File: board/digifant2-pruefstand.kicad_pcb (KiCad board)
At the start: 2 copper layers, 144 x 169 mm, 63 parts, among them J0 VW ECU HARNESS, J1 12V BENCH IN, J2 IDLE VALVE N71, J3 OLED / UI I2C, Q1 2N7002, Q2 P-MOS -30V >=5A, Q3 2N7002, Q5 2N7002, SW1 PUSH, SW2 PUSH, SW3 PUSH, U1 INA226 (0x40), U2 MCP4728 (0x60), U3 INA226 (0x41), U4 AD9833, U5 Raspberry Pi Pico, U6 TS5A3159A, U7 TS5A3159A, U8 TS5A3159A, Y1 25MHz

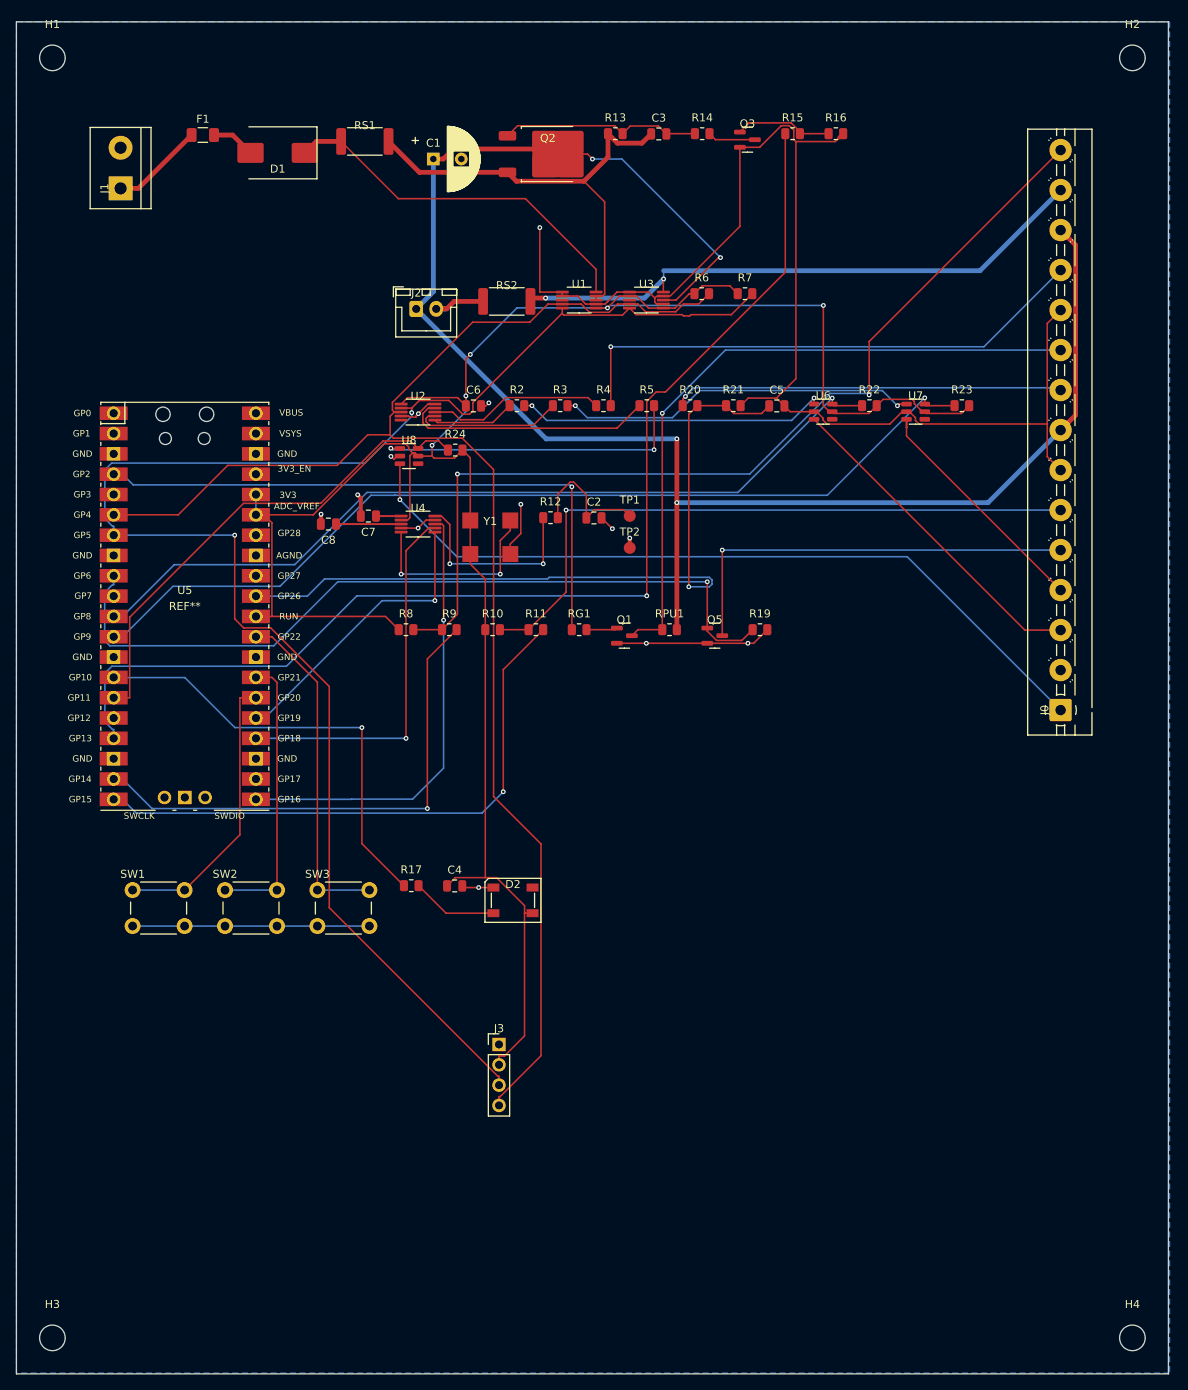
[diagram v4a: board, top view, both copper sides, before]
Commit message: Add 12 scope-probe test points (TP3-TP14) for firmware debugging
Bare 1.5mm test pads (same TestPoint_Pad_D1.5mm footprint as the knock
output's TP1/TP2) on the signals most likely to get probed while
debugging: crank drive, idle-switch drive, ignition/injector capture,
the AD9833 SPI bus (CS/SCK/MOSI), the I2C bus (SDA/SCL), the status LED
data line, and both 12V rails (sensed + switched).

Placement used an automated collision check (footprint + track distance)
against the real board, not manual trial and error -- 12 of 13 originally
attempted points cleared on the first or second pass. +3V3 was dropped
after 4 different anchor attempts (3 different Pico pins, then a
decoupling cap elsewhere) all routed through the same congested corridor
near the Pico; not worth forcing given +3V3 is already exposed at many
existing component pins.

Added digifant2_pruefstand.py's debug_test_points() and spliced the
corresponding schematic symbols/labels into the committed schematic
(verified ERC-clean and schematic-PCB parity unchanged from baseline) --
same lesson as the RS2 fix: a PCB-only addition would silently disappear
on the next schematic sync.

One real residual: TP12 (LED data) reopened a shorting_items/clearance
pair against GND. The actual pad-to-pad distances involved are ~2mm --
nowhere near a real clearance violation -- so the true conflict is
somewhere along the newly-routed copper itself, not locatable precisely
by script. Left for the same manual-nudge treatment as this board's
other tight pockets; KiCad's interactive router will show the exact
offending trace visually.

Co-Authored-By: Claude Sonnet 5 <noreply@anthropic.com>
Claude-Session: https://claude.ai/code/session_01XcEuUwwCT37oProAm8HYeY
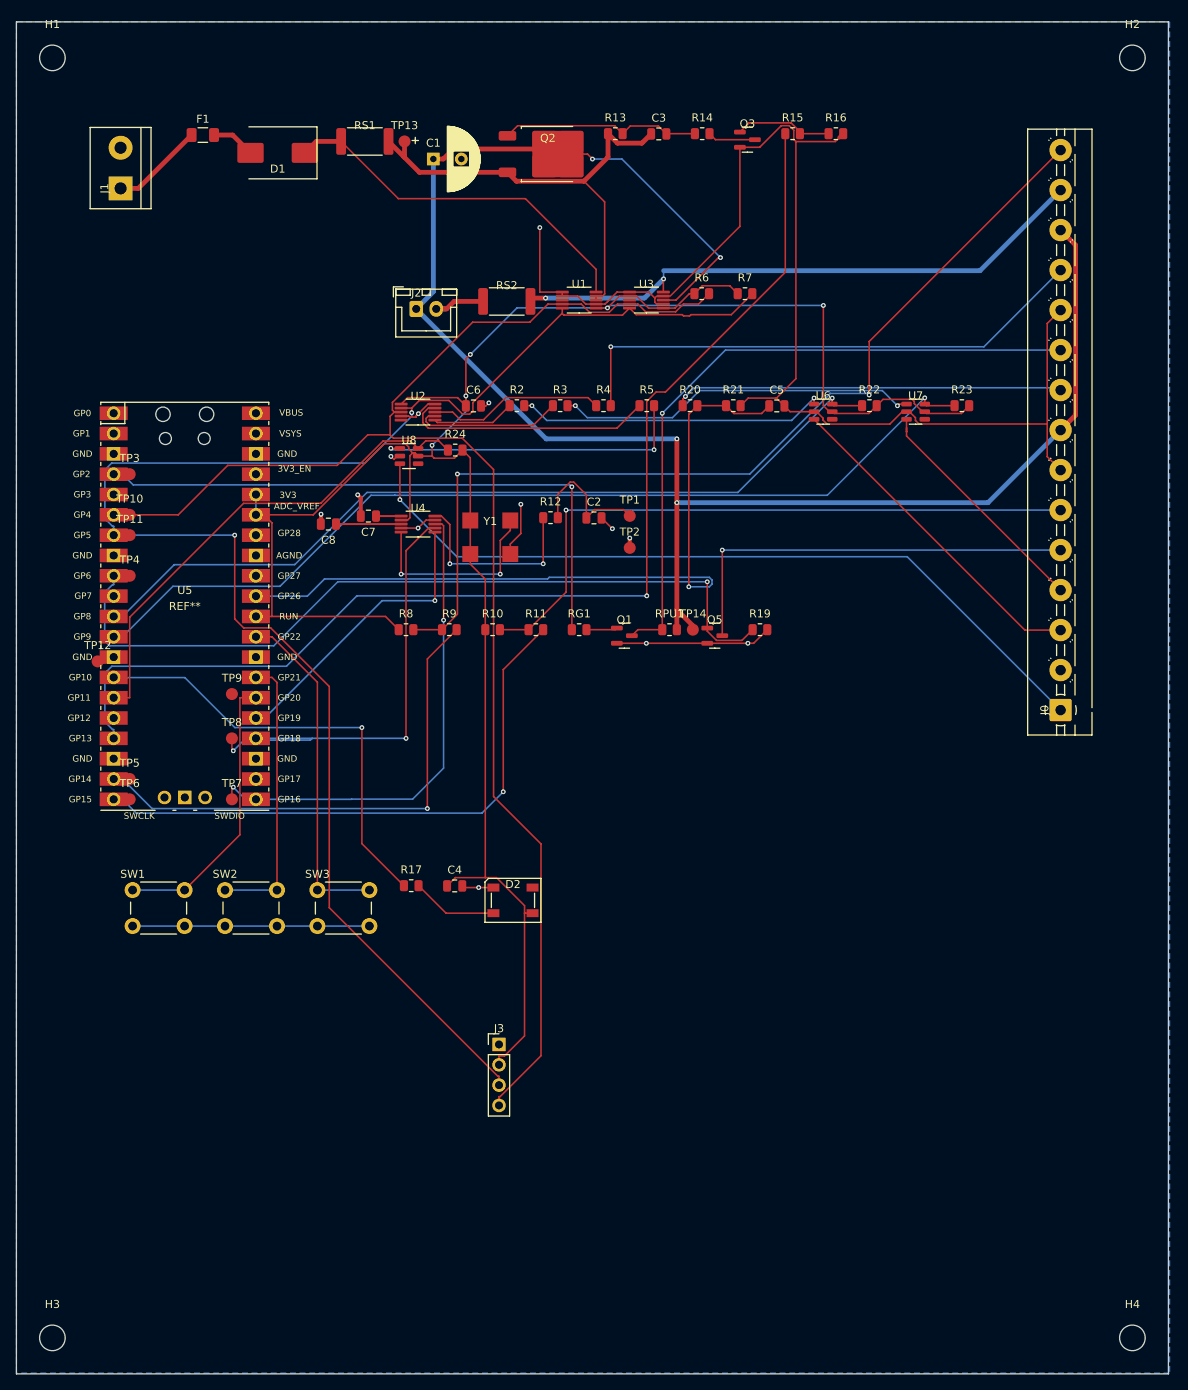
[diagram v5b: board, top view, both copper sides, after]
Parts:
- added TP10: TP I2C_SDA, TestPoint:TestPoint_Pad_D1.5mm, F.Cu at (14.2, 61.6)
- added TP11: TP I2C_SCL, TestPoint:TestPoint_Pad_D1.5mm, F.Cu at (14.2, 64.2)
- added TP12: TP GP10_LED_DATA, TestPoint:TestPoint_Pad_D1.5mm, F.Cu at (10.2, 79.9)
- added TP13: TP +12V_ECU, TestPoint:TestPoint_Pad_D1.5mm, F.Cu at (48.5, 14.9)
- added TP14: TP +12V_ECU_SW, TestPoint:TestPoint_Pad_D1.5mm, F.Cu at (84.6, 76.0)
- added TP3: TP GP2_CRANK, TestPoint:TestPoint_Pad_D1.5mm, F.Cu at (14.2, 56.5)
- added TP4: TP GP6_THROTTLE_IDLE_SW, TestPoint:TestPoint_Pad_D1.5mm, F.Cu at (14.2, 69.2)
- added TP5: TP GP14_IGN_CAPTURE, TestPoint:TestPoint_Pad_D1.5mm, F.Cu at (14.2, 94.6)
- added TP6: TP GP15_INJ_CAPTURE, TestPoint:TestPoint_Pad_D1.5mm, F.Cu at (14.2, 97.2)
- added TP7: TP GP16_SPI_CS, TestPoint:TestPoint_Pad_D1.5mm, F.Cu at (26.9, 97.2)
- added TP8: TP GP18_SPI_SCK, TestPoint:TestPoint_Pad_D1.5mm, F.Cu at (26.9, 89.6)
- added TP9: TP GP19_SPI_MOSI, TestPoint:TestPoint_Pad_D1.5mm, F.Cu at (26.9, 84.0)
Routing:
- net GP18_SPI_SCK: track 47.0 -> 59.1 mm, vias 1 -> 2
- net GP16_SPI_CS: track 56.5 -> 61.6 mm, vias 1 -> 2
- net +12V_ECU_SW: track 220.6 -> 223.9 mm
- net GP6_THROTTLE_IDLE_SW: track 100.4 -> 102.4 mm
- net GP2_CRANK: track 75.8 -> 77.8 mm
- net GP15_INJ_CAPTURE: track 72.8 -> 74.8 mm
- net GP14_IGN_CAPTURE: track 64.6 -> 66.6 mm
- net I2C_SCL: track 204.0 -> 206.0 mm
- net +12V_ECU: track 56.9 -> 58.8 mm
- net VW_PIN10: track 30.4 -> 29.8 mm

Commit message: Fix test points: real THT footprint, and move 10 out from under the Pico
Two real defects caught by user review of the previous commit:

1. All 14 test points (TP1-TP14) used TestPoint_Pad_D1.5mm, a bare SMD
   pad with no drill -- not THT as documented/intended. Switched to
   TestPoint_THTPad_D1.5mm_Drill0.7mm (real 0.7mm hole), vendored the
   footprint, and updated fetch_libs.sh.

2. TP3-TP12 were anchored right at their signal's own Pico pin, which
   placed 10 of the 12 physically *underneath* the Pico module's real
   footprint courtyard (x:[10,32.1] y:[47,99.1]) -- completely
   unreachable with a probe once the module is soldered on. Moved them
   to the clear margin strip west of the Pico (x=5mm), verified against
   real board-edge and courtyard geometry, not just pad/track proximity.

Along the way, found and fixed a real bug in this session's own PCB
scripts: pcbnew.FOOTPRINT(template) clones inherit the template's UUID
unless explicitly reset, so every footprint cloned this way (C7/C8, and
all of TP1-TP14, since they were all cloned from one template) shared a
UUID with its siblings. This doesn't break electrical connectivity but
corrupts DRC's item-identity tracking -- several "violations" this
session were real defects reported against the wrong footprint (one
report cited two parts 70mm apart as a courtyard overlap). Fixed with
ResetUuid() on every affected footprint and pad. With correct UUIDs,
DRC now correctly identified two genuine issues (TP1 too close to a
VW_PIN12 trace once it had a real drill hole; TP13's courtyard actually
overlapping RS1's) that had been reported against the wrong parts
before -- both repositioned and reverified.

Co-Authored-By: Claude Sonnet 5 <noreply@anthropic.com>
Claude-Session: https://claude.ai/code/session_01XcEuUwwCT37oProAm8HYeY
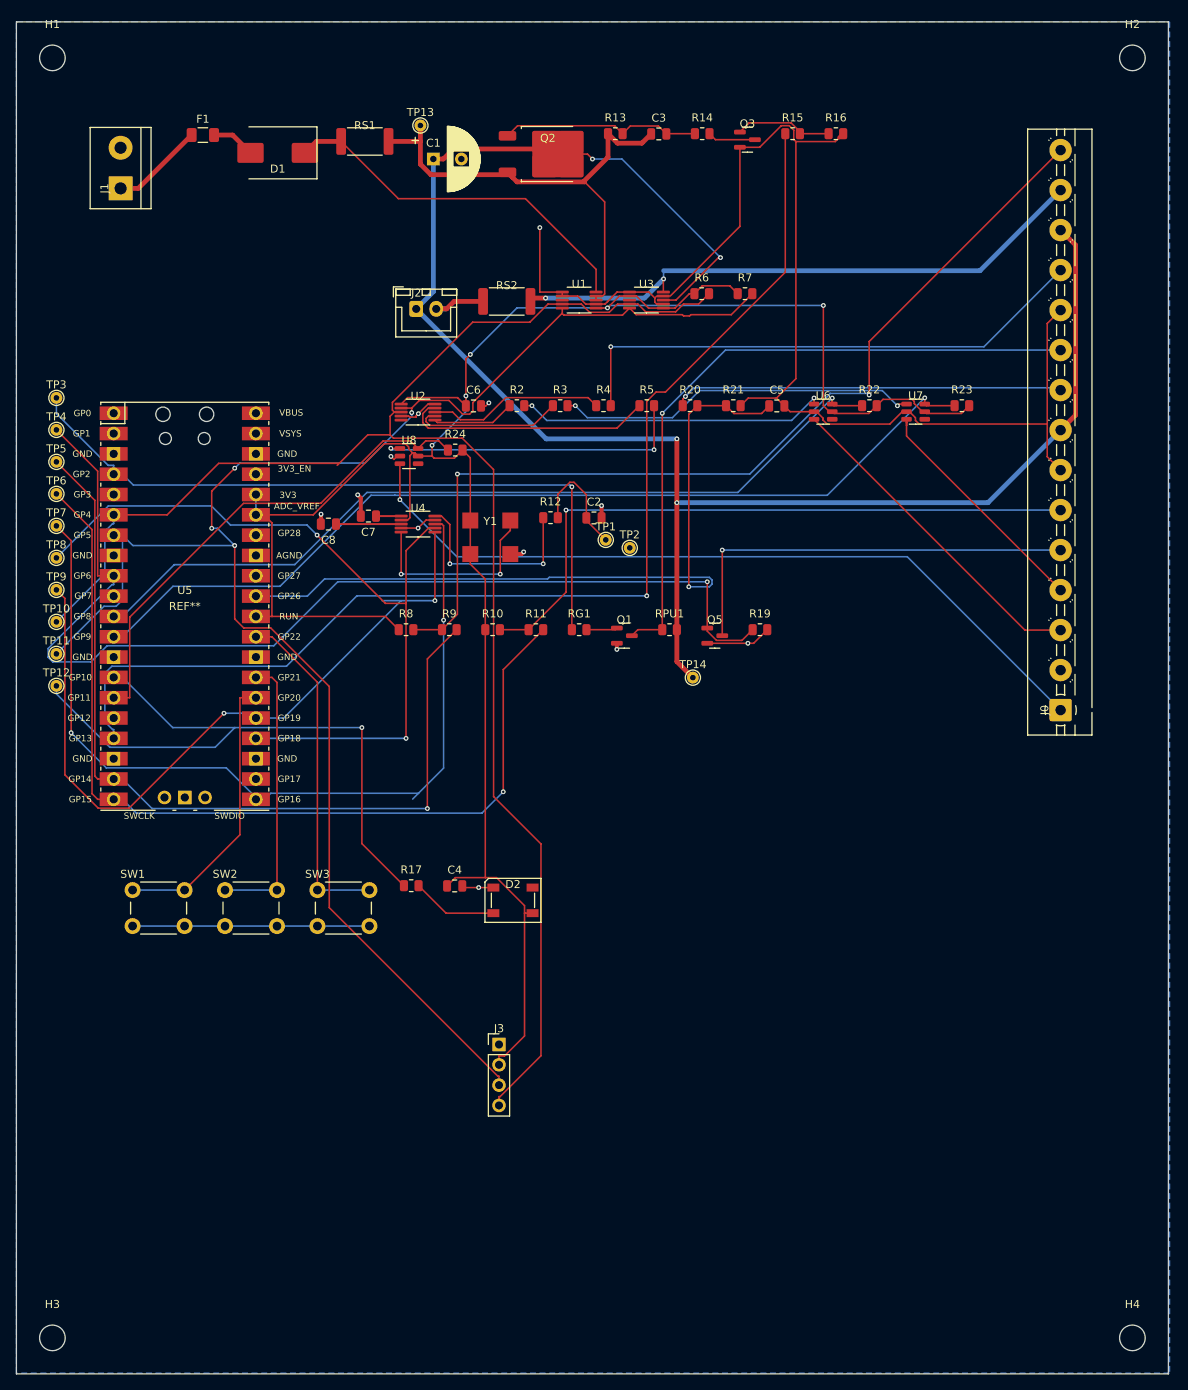
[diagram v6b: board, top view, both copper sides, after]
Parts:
- TP1, TP10, TP11, TP12, TP13, TP14, TP2, TP3, TP4, TP5, TP6, TP7, TP8, TP9: footprint TestPoint:TestPoint_Pad_D1.5mm -> TestPoint:TestPoint_THTPad_D1.5mm_Drill0.7mm
- moved TP5 40.7 mm to (5.00, 55.0)
- moved TP7 40.6 mm to (5.00, 63.0)
- moved TP6 39.3 mm to (5.00, 59.0)
- moved TP8 31.5 mm to (5.00, 67.0)
- moved TP9 25.5 mm to (5.00, 71.0)
- moved TP4 20.4 mm to (5.00, 51.0)
- moved TP11 17.4 mm to (5.00, 79.0)
- moved TP10 16.2 mm to (5.00, 75.0)
- moved TP3 13.2 mm to (5.00, 47.0)
- moved TP12 6.00 mm to (5.00, 83.0)
- moved TP14 6.00 mm to (84.6, 82.0)
- moved TP1 4.24 mm to (73.7, 64.8)
- moved TP13 2.81 mm to (50.5, 12.9)
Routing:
- net GP19_SPI_MOSI: track 37.0 -> 93.7 mm, vias 1 -> 2
- net GP16_SPI_CS: track 61.6 -> 111.0 mm
- net GP14_IGN_CAPTURE: track 66.6 -> 108.4 mm
- net GP15_INJ_CAPTURE: track 74.8 -> 115.2 mm
- net GP18_SPI_SCK: track 59.1 -> 98.5 mm
- net GP6_THROTTLE_IDLE_SW: track 102.4 -> 135.7 mm
- net GP10_LED_DATA: track 55.6 -> 82.6 mm
- net GND: track 240.6 -> 223.5 mm, vias 13 -> 12
- net I2C_SDA: track 189.7 -> 206.5 mm
- net GP2_CRANK: track 77.8 -> 88.7 mm
- net I2C_SCL: track 206.0 -> 209.8 mm, vias 2 -> 4
- net +12V_ECU_SW: track 223.9 -> 227.4 mm
- net U4_LOAD: track 16.8 -> 14.4 mm
- net +12V_ECU: track 58.8 -> 61.1 mm

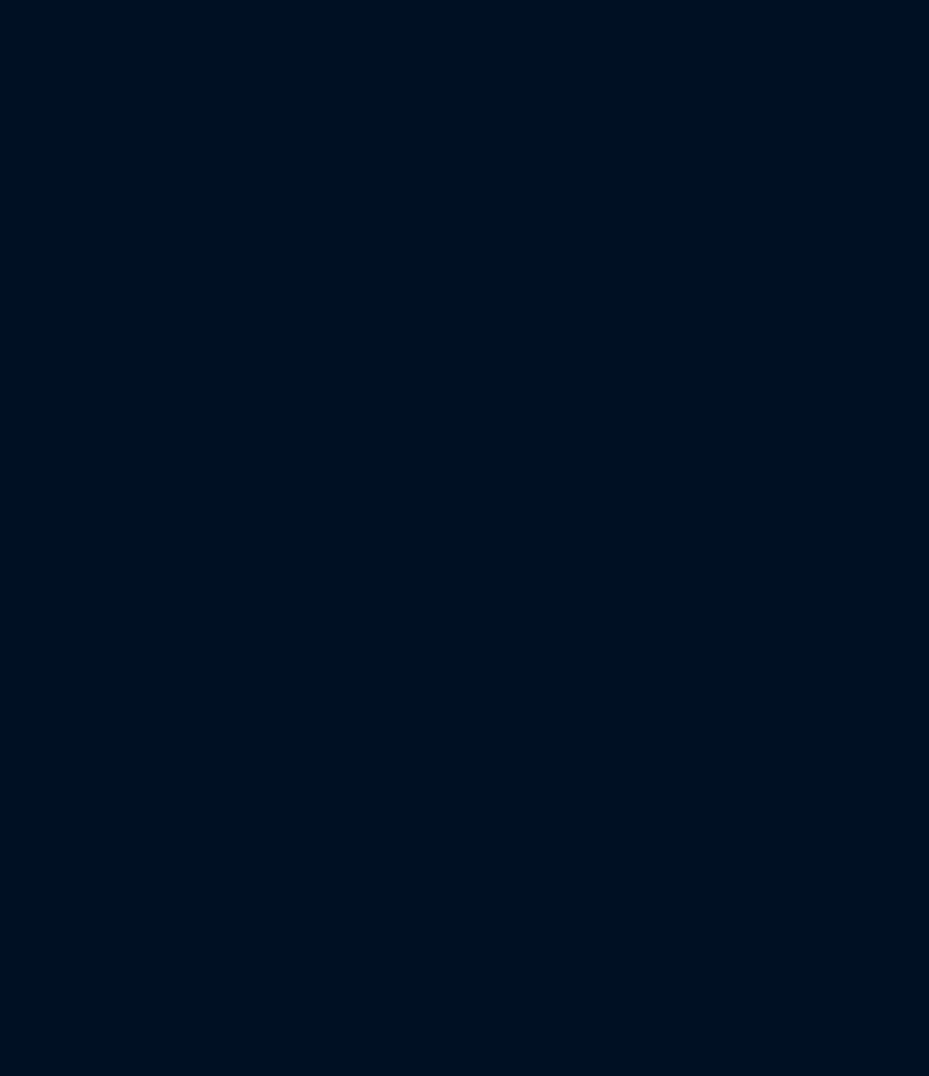
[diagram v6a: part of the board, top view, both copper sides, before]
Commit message: Add a 12x16 THT proto area (PROTO1) in the empty space by J0
Perfboard-style prototyping grid: 192 isolated 1.6mm/0.8mm-drill pads
on 2.54mm (0.1") pitch, ~30x38mm, placed in the large empty area
bottom-right of the board (below J0's footprint, clear of the H4
mounting hole's keepout). Each pad is its own net -- solder in whatever
you need for one-off additions or bodge wires, same idea as a classic
protoboard section.

PCB-only, same treatment as the mounting holes: no schematic symbol,
since it isn't part of the actual circuit. Verified DRC-neutral (zone
refilled so the GND pour properly isolates each pad; the one new
DRC line is an expected extra_footprint warning, matching what H1-H4
would also show without their BOM/pos-file exclusion attributes).

Co-Authored-By: Claude Sonnet 5 <noreply@anthropic.com>
Claude-Session: https://claude.ai/code/session_01XcEuUwwCT37oProAm8HYeY
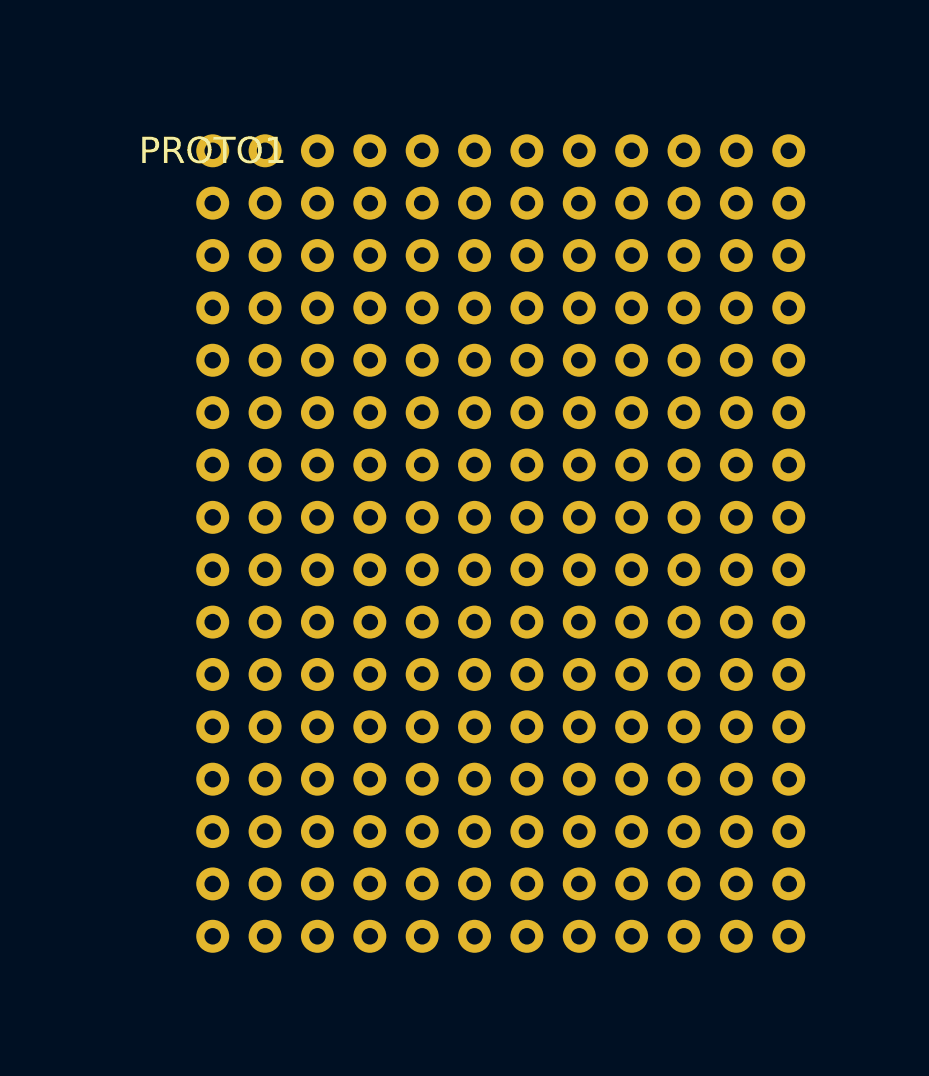
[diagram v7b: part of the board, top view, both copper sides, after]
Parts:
- added PROTO1: PROTO AREA, , F.Cu at (92.0, 97.0)
